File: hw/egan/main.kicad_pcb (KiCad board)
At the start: 2 copper layers, 59.7 x 17.8 mm, 28 parts, among them J1 Conn_02x06_Odd_Even, J2 Conn_01x01_Pin, J3 Conn_01x01_Pin, J4 Conn_01x01_Pin, Q1 LMG5200, U1 INA240A3PW, U2 ADS7042xDCU, U3 ADS7042xDCU

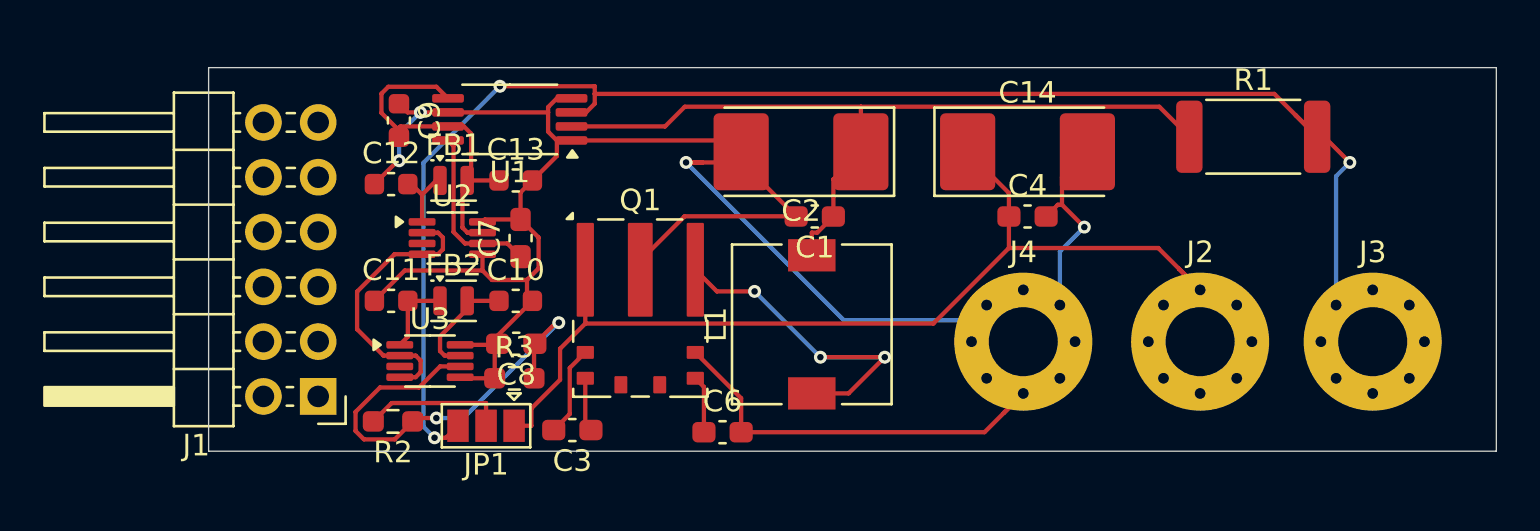
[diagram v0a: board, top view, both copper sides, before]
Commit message: add PMOD pinout. mostly inspired by runger's table.
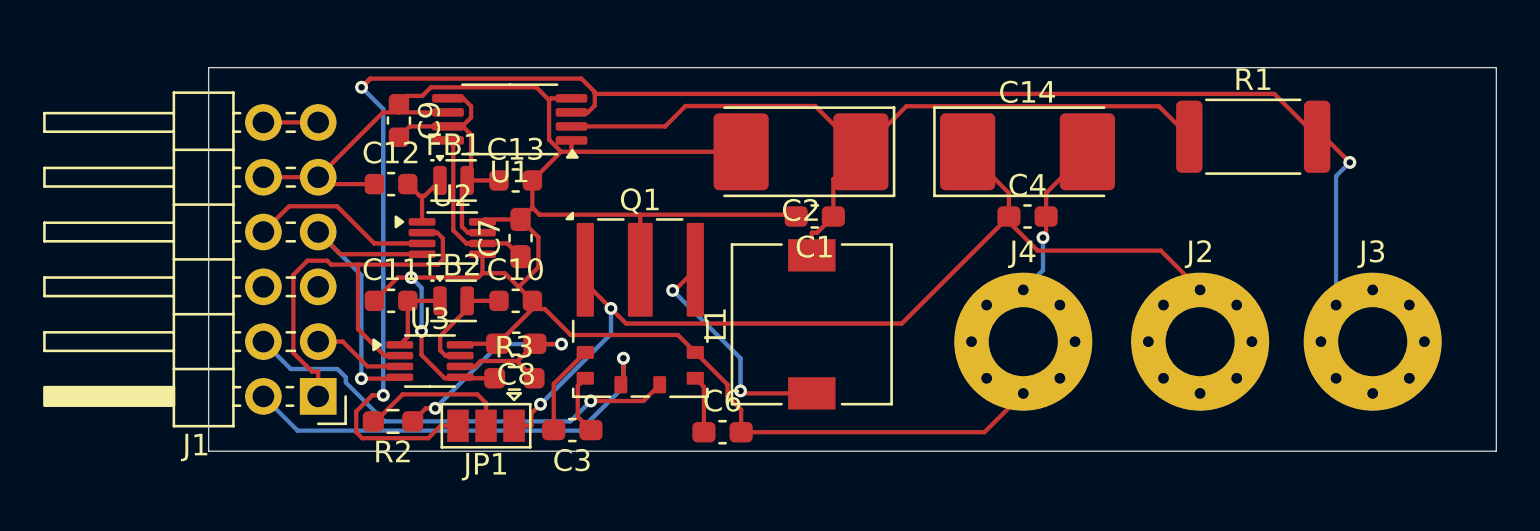
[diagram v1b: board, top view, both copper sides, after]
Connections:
- J1 pad 1: unconnected-(J1-Pin_1-Pad1) -> Net-(J1-Pin_1)
- J1 pad 10: unconnected-(J1-Pin_10-Pad10) -> GND
- J1 pad 11: unconnected-(J1-Pin_11-Pad11) -> VCC3V3
- J1 pad 12: unconnected-(J1-Pin_12-Pad12) -> VCC3V3
- J1 pad 2: unconnected-(J1-Pin_2-Pad2) -> Net-(J1-Pin_2)
- J1 pad 3: unconnected-(J1-Pin_3-Pad3) -> Net-(J1-Pin_3)
- J1 pad 4: unconnected-(J1-Pin_4-Pad4) -> Net-(J1-Pin_4)
- J1 pad 7: unconnected-(J1-Pin_7-Pad7) -> Net-(J1-Pin_7)
- J1 pad 8: unconnected-(J1-Pin_8-Pad8) -> Net-(J1-Pin_8)
- J1 pad 9: unconnected-(J1-Pin_9-Pad9) -> GND
- Q1 pad 4: unconnected-(Q1-HI-Pad4) -> Net-(J1-Pin_2)
- Q1 pad 5: unconnected-(Q1-LI-Pad5) -> Net-(J1-Pin_4)
- U2 pad 2: Net-(U2-SCLK) -> Net-(J1-Pin_1)
- U2 pad 3: unconnected-(U2-SDO-Pad3) -> Net-(J1-Pin_8)
- U2 pad 4: Net-(U2-SCLK) -> Net-(J1-Pin_7)
- U3 pad 2: Net-(U2-SCLK) -> Net-(J1-Pin_1)
- U3 pad 3: unconnected-(U3-SDO-Pad3) -> Net-(J1-Pin_3)
- U3 pad 4: Net-(U2-SCLK) -> Net-(J1-Pin_7)
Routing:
- net Net-(J1-Pin_1): track 0.00 -> 21.2 mm
- net Net-(J1-Pin_2): track 0.00 -> 20.8 mm, vias 0 -> 1
- net Net-(J1-Pin_4): track 0.00 -> 20.7 mm, vias 0 -> 1
- net Net-(J1-Pin_7): track 0.00 -> 14.7 mm, vias 0 -> 1
- net Net-(U2-SCLK): track 13.3 -> 0.00 mm
- net Net-(J1-Pin_8): track 0.00 -> 8.56 mm
- net Net-(J3-Pin_1): track 90.7 -> 98.2 mm
- net Net-(L1-Pad1): track 17.5 -> 10.8 mm, vias 3 -> 2
- net Net-(U3-AINP): track 21.8 -> 15.4 mm
- net Net-(J1-Pin_3): track 0.00 -> 4.26 mm
- net Net-(U1-REF1): track 16.3 -> 13.1 mm
- net Net-(J2-Pin_1): track 65.2 -> 62.6 mm, vias 0 -> 2
- net VCC3V3: track 0.00 -> 2.54 mm
- net GND: track 133.0 -> 131.9 mm, vias 4 -> 3

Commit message: Add 5V charge-pump
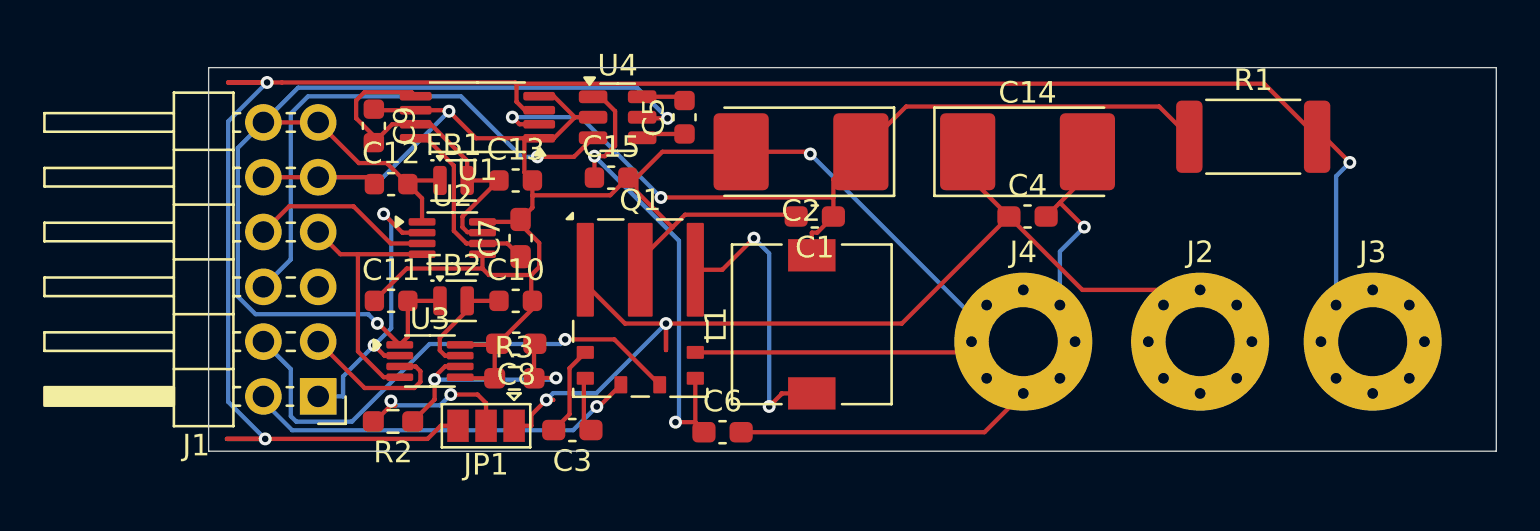
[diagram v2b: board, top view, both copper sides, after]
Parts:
- added C15: 1uF, Capacitor_SMD:C_0603_1608Metric, F.Cu at (148.2, 106.7)
- added C5: 1uF, Capacitor_SMD:C_0603_1608Metric, F.Cu at (151.6, 103.9)
- added U4: AP3602A, Package_TO_SOT_SMD:TSOT-23-6, F.Cu at (148.5, 103.9)
- moved U1 1.50 mm to (142.0, 103.9)
- moved C9 1.19 mm to (137.2, 104.3)
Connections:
- net Net-(Q1-VCC) renamed VCC5V
- C11 pad 2: Net-(U3-DVDD) -> VCC3V3
- C12 pad 2: Net-(U2-DVDD) -> VCC3V3
- FB1 pad 1: Net-(U2-DVDD) -> VCC3V3
- FB2 pad 1: Net-(U3-DVDD) -> VCC3V3
- J1 pad 6: unconnected-(J1-Pin_6-Pad6) -> Net-(J1-Pin_6)
- U2 pad 1: Net-(U2-DVDD) -> VCC3V3
- U3 pad 1: Net-(U3-DVDD) -> VCC3V3
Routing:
- net VCC3V3: track 2.54 -> 53.3 mm, vias 0 -> 2
- net Net-(J1-Pin_6): track 0.00 -> 24.4 mm, vias 0 -> 1
- net Net-(J3-Pin_1): track 98.2 -> 119.7 mm
- net VCC5V: track 2.67 -> 23.6 mm, vias 0 -> 2
- net GND: track 131.9 -> 142.2 mm
- net Net-(J1-Pin_1): track 21.2 -> 14.2 mm, vias 0 -> 2
- net Net-(J2-Pin_1): track 62.6 -> 67.8 mm
- net Net-(U1-REF1): track 13.1 -> 16.9 mm
- net Net-(J1-Pin_4): track 20.7 -> 24.5 mm
- net Net-(U3-DVDD): track 3.69 -> 0.00 mm
- net Net-(U3-AINP): track 15.4 -> 12.2 mm
- net Net-(U2-DVDD): track 3.22 -> 0.00 mm
- net Net-(U1-+): track 37.3 -> 40.4 mm, vias 0 -> 2
- net Net-(J1-Pin_3): track 4.26 -> 7.29 mm
- net Net-(L1-Pad1): track 10.8 -> 13.7 mm
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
